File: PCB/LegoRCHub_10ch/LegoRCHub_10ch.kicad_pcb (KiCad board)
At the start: 2 copper layers, 39.3 x 55.2 mm, 41 parts, among them J1 Conn_01x02, J10 Conn_01x03, J11 Conn_01x03_MountingPin, J12 Conn_01x02, J13 Conn_01x02, J2 Conn_01x02, J3 Conn_01x02, J4 Conn_01x02, J5 Conn_01x02, J6 Conn_01x02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

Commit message: Added project LegoRCHub_10ch: (beta 2): changed pins to screw terminals
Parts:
- J1, J2, J3, J4, J5, J6: footprint Connector_PinHeader_2.54mm:PinHeader_1x02_P2.54mm_Vertical -> TerminalBlock_Phoenix:TerminalBlock_Phoenix_MPT-0,5-2-2.54_1x02_P2.54mm_Horizontal
- moved J5 2.81 mm to (28.2, 66.8), turned to 90 degrees
- moved J4 2.81 mm to (60.7, 46.5), turned to -90 degrees
- moved J6 2.81 mm to (60.7, 58.3), turned to -90 degrees
- moved J3 2.81 mm to (28.2, 55.1), turned to 90 degrees
- moved J1 2.81 mm to (28.2, 43.3), turned to 90 degrees
- moved J2 2.79 mm to (60.7, 34.8), turned to -90 degrees
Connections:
- J1 pad 1: Net-(J1-Pad1) -> Net-(U1-Pad8)
- J1 pad 2: Net-(J1-Pad2) -> Net-(U1-Pad6)
- J3 pad 1: Net-(J3-Pad1) -> Net-(U3-Pad8)
- J4 pad 1: Net-(J4-Pad1) -> Net-(U4-Pad8)
- J5 pad 1: Net-(U5-Pad6) -> Net-(U5-Pad8)
- J5 pad 2: Net-(U5-Pad8) -> Net-(J5-Pad2)
- J6 pad 1: Net-(U6-Pad6) -> Net-(U6-Pad8)
- J6 pad 2: Net-(U6-Pad8) -> Net-(J6-Pad2)
- U1 pad 6: Net-(J1-Pad1) -> Net-(U1-Pad6)
- U1 pad 8: Net-(J1-Pad2) -> Net-(U1-Pad8)
- U2 pad 6: Net-(J2-Pad1) -> Net-(J2-Pad2)
- U2 pad 8: Net-(J2-Pad2) -> Net-(J2-Pad1)
- U3 pad 6: Net-(J3-Pad1) -> Net-(J3-Pad2)
- U3 pad 8: Net-(J3-Pad2) -> Net-(U3-Pad8)
- U4 pad 6: Net-(J4-Pad1) -> Net-(J4-Pad2)
- U4 pad 8: Net-(J4-Pad2) -> Net-(U4-Pad8)
- U5 pad 6: Net-(U5-Pad6) -> Net-(J5-Pad2)
- U6 pad 6: Net-(U6-Pad6) -> Net-(J6-Pad2)
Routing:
- net Net-(J5-Pad2): track 0.00 -> 2.92 mm
- net Net-(U4-Pad8): track 0.00 -> 2.92 mm
- net Net-(U3-Pad8): track 0.00 -> 2.92 mm
- net Net-(U1-Pad8): track 0.00 -> 2.92 mm
- net Net-(U1-Pad6): track 0.00 -> 2.92 mm
- net Net-(J6-Pad2): track 0.00 -> 2.92 mm
- net Net-(J1-Pad1): track 2.68 -> 0.00 mm
- net Net-(J1-Pad2): track 2.68 -> 0.00 mm
- net Net-(U6-Pad6): track 2.68 -> 0.00 mm
- net Net-(J4-Pad1): track 2.68 -> 0.00 mm
- net Net-(U5-Pad6): track 2.68 -> 0.00 mm
- net Net-(J3-Pad1): track 2.68 -> 0.00 mm

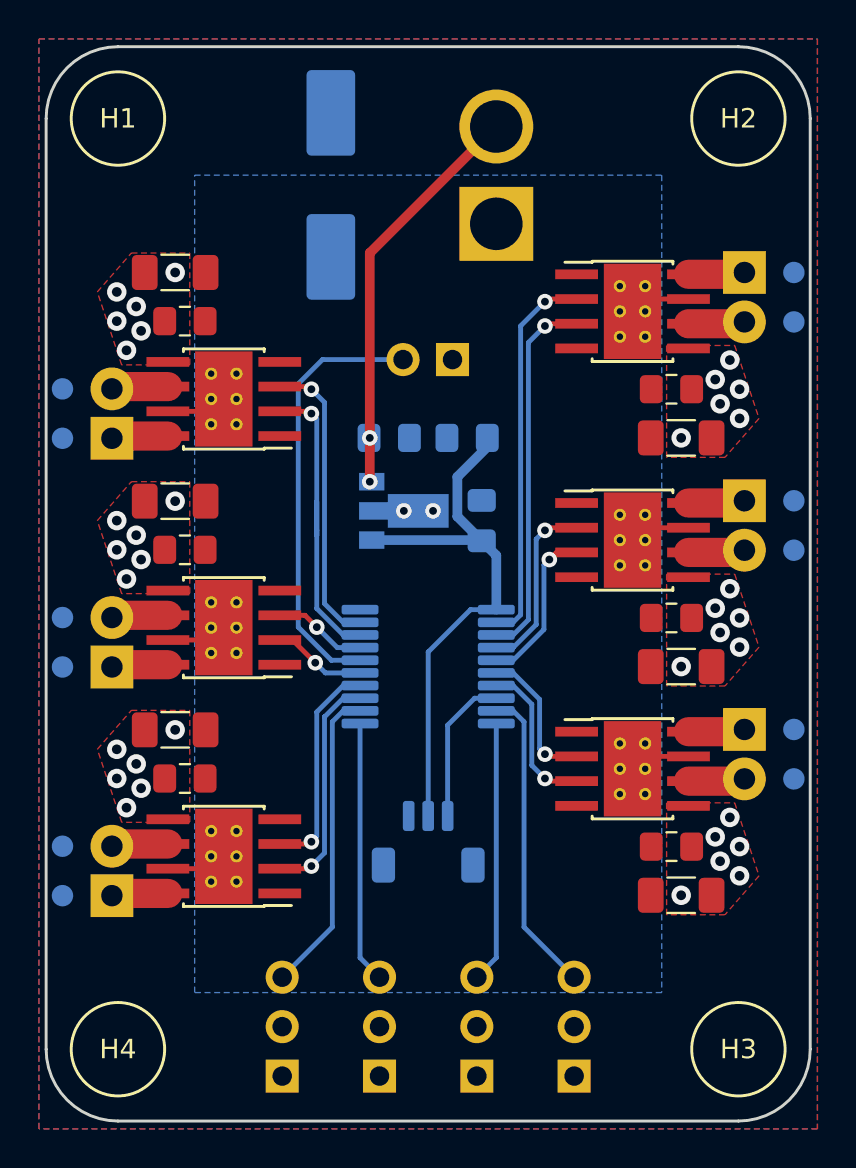
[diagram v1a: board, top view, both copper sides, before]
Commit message: LegoRCHub_10ch: ...
Revert "LegoRCHub_10ch: ..."

This reverts commit a8209f8826470efcec7313ecef0b47345458ad62.
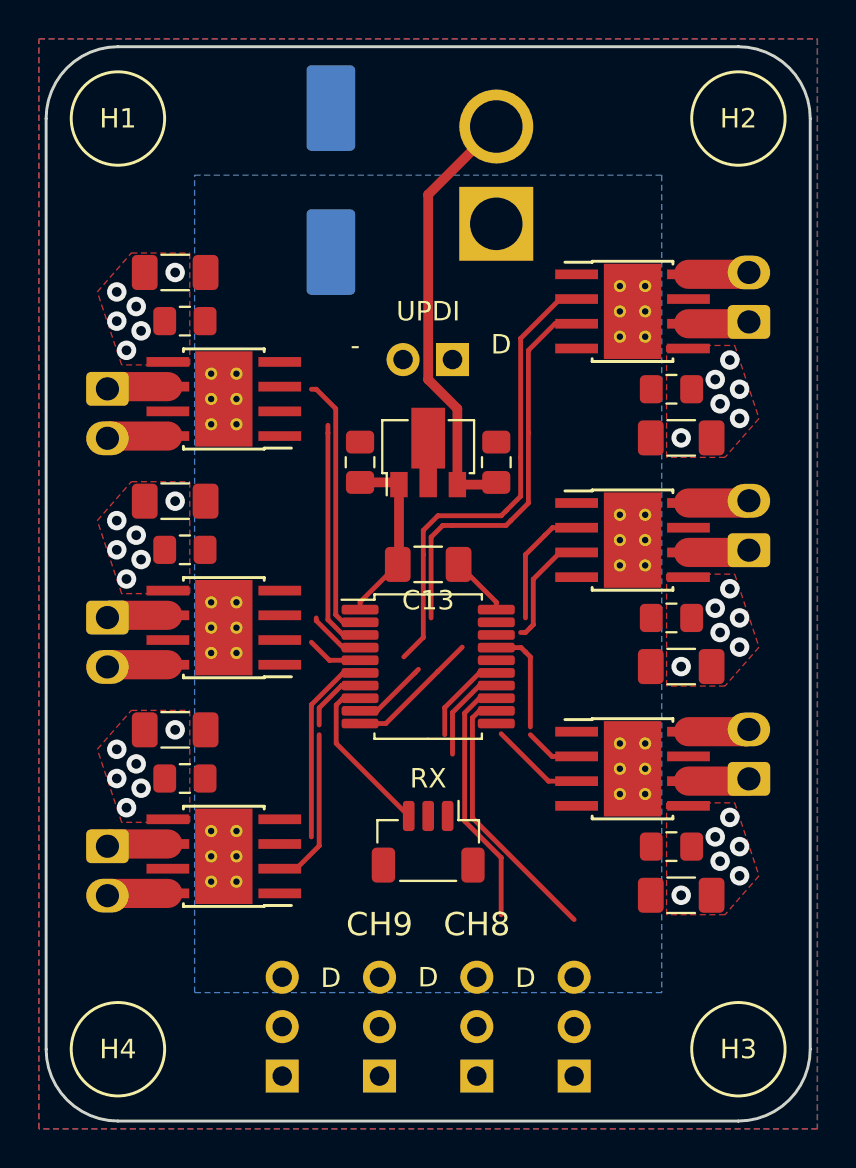
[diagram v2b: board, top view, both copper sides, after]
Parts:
- C13: footprint Capacitor_SMD:C_0805_2012Metric_Pad1.18x1.45mm_HandSolder -> Capacitor_SMD:C_1206_3216Metric_Pad1.33x1.80mm_HandSolder; moved to F.Cu
- C14, C15, J11, U7, U8: moved to F.Cu
- J1, J2, J3, J4, J5, J6: footprint TerminalBlock_Phoenix:TerminalBlock_Phoenix_MPT-0,5-2-2.54_1x02_P2.54mm_Horizontal -> Connector_Molex:Molex_KK-254_AE-6410-02A_1x02_P2.54mm_Vertical
- moved C14 5.64 mm to (48.0, 44.5), turned to -90 degrees
- moved C15 5.64 mm to (41.0, 44.5), turned to -90 degrees
- moved C13 3.55 mm to (44.5, 49.8), turned to 180 degrees
- moved U8 3.25 mm to (44.5, 44.0), turned to 90 degrees
- moved J5 2.55 mm to (28.0, 64.3), turned to -90 degrees
- moved J2 2.55 mm to (60.9, 37.3), turned to 90 degrees
- moved J1 2.55 mm to (28.0, 40.8), turned to -90 degrees
- moved J3 2.55 mm to (28.0, 52.5), turned to -90 degrees
- moved J4 2.55 mm to (60.9, 49.1), turned to 90 degrees
- moved J6 2.55 mm to (60.9, 60.8), turned to 90 degrees
- moved C16 0.25 mm to (39.5, 30.1)
- turned J11 to 180 degrees
- turned U7 to 0 degrees
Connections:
- J1 pad 1: Net-(U1-Pad8) -> Net-(U1-Pad6)
- J1 pad 2: Net-(U1-Pad6) -> Net-(J1-Pad2)
- J3 pad 1: Net-(U3-Pad8) -> Net-(U3-Pad6)
- J4 pad 1: Net-(U4-Pad8) -> Net-(U4-Pad6)
- J5 pad 1: Net-(U5-Pad8) -> Net-(U5-Pad6)
- J6 pad 1: Net-(U6-Pad8) -> Net-(U6-Pad6)
- U1 pad 8: Net-(U1-Pad8) -> Net-(J1-Pad2)
- U2 pad 6: Net-(J2-Pad2) -> Net-(J2-Pad1)
- U2 pad 8: Net-(J2-Pad1) -> Net-(J2-Pad2)
- U3 pad 6: Net-(J3-Pad2) -> Net-(U3-Pad6)
- U3 pad 8: Net-(U3-Pad8) -> Net-(J3-Pad2)
- U4 pad 6: Net-(J4-Pad2) -> Net-(U4-Pad6)
- U4 pad 8: Net-(U4-Pad8) -> Net-(J4-Pad2)
- U5 pad 6: Net-(J5-Pad2) -> Net-(U5-Pad6)
- U5 pad 8: Net-(U5-Pad8) -> Net-(J5-Pad2)
- U6 pad 6: Net-(J6-Pad2) -> Net-(U6-Pad6)
- U6 pad 8: Net-(U6-Pad8) -> Net-(J6-Pad2)
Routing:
- net /UPDI: track 22.3 -> 0.00 mm
- net VCC: track 28.3 -> 9.30 mm
- net /CH2_2: track 19.7 -> 38.1 mm, vias 1 -> 0
- net /CH1_2: track 16.6 -> 0.00 mm, vias 1 -> 0
- net /CH1_3: track 15.2 -> 0.00 mm, vias 1 -> 0
- net /CH2_3: track 19.1 -> 32.7 mm, vias 1 -> 0
- net /CH8: track 13.4 -> 0.00 mm
- net /CH10: track 15.8 -> 3.88 mm
- net /CH5_2: track 11.9 -> 21.3 mm, vias 1 -> 0
- net /CH9: track 13.4 -> 6.88 mm
- net GND: track 9.54 -> 3.13 mm, vias 2 -> 0
- net /CH5_3: track 11.2 -> 4.96 mm, vias 1 -> 0
- net /CH6_2: track 7.39 -> 12.8 mm, vias 1 -> 0
- net Net-(U3-Pad6): track 0.00 -> 3.15 mm
- net Net-(J1-Pad2): track 0.00 -> 3.15 mm
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
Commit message: LegoRCHub_10ch: ...
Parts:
- J11: moved to B.Cu
- moved J11 35.2 mm to (51.5, 29.6)
- moved J13 3.26 mm to (44.7, 32.0)
- moved C16 2.51 mm to (37.0, 29.8)
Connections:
- U7 pad 10: /CH9 -> /CH5_2
- U7 pad 11: /CH8 -> /CH6_3
- U7 pad 12: /CH7 -> unconnected-(U7-Pad12)
- U7 pad 13: /CH5_2 -> unconnected-(U7-Pad13)
- U7 pad 14: /CH5_3 -> unconnected-(U7-Pad14)
- U7 pad 15: /CH3_2 -> unconnected-(U7-Pad15)
- U7 pad 17: /CH3_3 -> /CH6_2
- U7 pad 18: /CH1_2 -> /CH4_3
- U7 pad 19: /CH1_3 -> /CH4_2
- U7 pad 2: /CH2_2 -> /CH1_3
- U7 pad 3: /CH2_3 -> /CH1_2
- U7 pad 4: /CH4_2 -> /CH3_3
- U7 pad 5: /CH4_3 -> /CH3_2
- U7 pad 6: /CH6_2 -> unconnected-(U7-Pad6)
- U7 pad 7: /CH6_3 -> unconnected-(U7-Pad7)
- U7 pad 9: /CH10 -> /CH5_3
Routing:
- net /CH2_2: track 38.1 -> 22.0 mm
- net /CH1_3: track 0.00 -> 14.9 mm
- net /CH1_2: track 0.00 -> 14.7 mm
- net /CH7: track 13.9 -> 0.00 mm
- net /CH2_3: track 32.7 -> 19.5 mm
- net /CH5_2: track 21.3 -> 10.1 mm
- net /IBus: track 8.61 -> 0.00 mm
- net /CH9: track 6.88 -> 0.00 mm
- net /CH5_3: track 4.96 -> 9.94 mm
- net /CH6_2: track 12.8 -> 8.65 mm
- net /CH10: track 3.88 -> 0.00 mm
- net /CH6_3: track 8.33 -> 5.35 mm
- net /CH4_2: track 9.41 -> 7.75 mm
- net /CH4_3: track 8.83 -> 7.49 mm
- net +BATT: track 22.5 -> 23.5 mm
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
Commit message: LegoRCHub_10ch: improved design - beta 1
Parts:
- removed the J12 at (45.7, 39.3)
- added J13: Conn_01x01, Connector_Wire:SolderWirePad_1x01_SMD_1x2mm, F.Cu at (42.0, 61.0)
- moved C16 15.2 mm to (52.2, 29.8)
- moved J11 14.1 mm to (37.7, 32.8)
- moved J8 10.0 mm to (52.0, 76.1)
- moved J10 5.00 mm to (47.0, 76.1)
- moved J9 5.00 mm to (42.0, 76.1)
- moved C14 1.00 mm to (48.0, 43.5)
- moved C15 1.00 mm to (41.0, 43.5)
- moved U8 1.00 mm to (44.5, 43.0)
- moved J12 0.25 mm to (44.5, 32.0)
- renumbered J13 to J12
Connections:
- U7 pad 12: unconnected-(U7-Pad12) -> /CH8
- U7 pad 13: unconnected-(U7-Pad13) -> /CH10
- U7 pad 14: unconnected-(U7-Pad14) -> /CH9
- U7 pad 15: unconnected-(U7-Pad15) -> /CH7
- U7 pad 6: unconnected-(U7-Pad6) -> /CH2_2
- U7 pad 7: unconnected-(U7-Pad7) -> /CH2_3
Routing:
- net /IBus: track 0.00 -> 26.8 mm, vias 0 -> 1
- net /CH7: track 0.00 -> 22.3 mm
- net /CH9: track 0.00 -> 18.0 mm
- net /CH8: track 0.00 -> 16.9 mm
- net VCC: track 9.70 -> 25.8 mm, vias 0 -> 1
- net /CH10: track 0.00 -> 15.8 mm
- net /UPDI: track 0.00 -> 9.94 mm
- net /CH2_3: track 19.5 -> 26.5 mm
- net /CH2_2: track 22.0 -> 25.9 mm
- net +BATT: track 23.5 -> 21.4 mm
- net /CH5_2: track 10.1 -> 8.54 mm
- net /CH6_3: track 5.35 -> 4.19 mm
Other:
- board text added: "+12V MAX"
- board text removed: "13V MAX"
